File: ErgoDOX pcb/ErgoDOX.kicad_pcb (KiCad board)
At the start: 2 copper layers, 182.8 x 158.9 mm, 65 parts, among them J1 USB, J2 3.5mm, J3 JMP, J4 JMP, SW0:10 SW0:3, SW0:11 SW0:2, SW0:12 SW0:1, SW0:7 SW0:6, SW0:8 SW0:5, SW0:9 SW0:4, SW1:10 SW1:3, SW1:11 SW1:2, SW1:12 SW1:1, SW1:13 SW1:0, SW1:9 SW1:4, SW2:10 SW2:3, SW2:11 SW2:2, SW2:12 SW2:1, SW2:13 SW2:0, SW2:7 SW2:6, SW2:8 SW2:5, SW2:9 SW2:4, SW3:10 SW3:3, SW3:11 SW3:2, SW3:12 SW3:1, SW3:13 SW3:0, SW3:8 SW3:5, SW3:9 SW3:4, SW4:10 SW4:3, SW4:11 SW4:2, SW4:12 SW4:1, SW4:13 SW4:0, SW4:7 SW4:6, SW4:8 SW4:5, SW4:9 SW4:4, SW5:10 SW5:3, SW5:11 SW5:2, SW5:12 SW5:1, SW5:13 SW5:0, SW5:7 SW5:6, SW5:8 SW5:5, SW5:9 SW5:4, U1 TEENSY2.0, U2 MCP23018

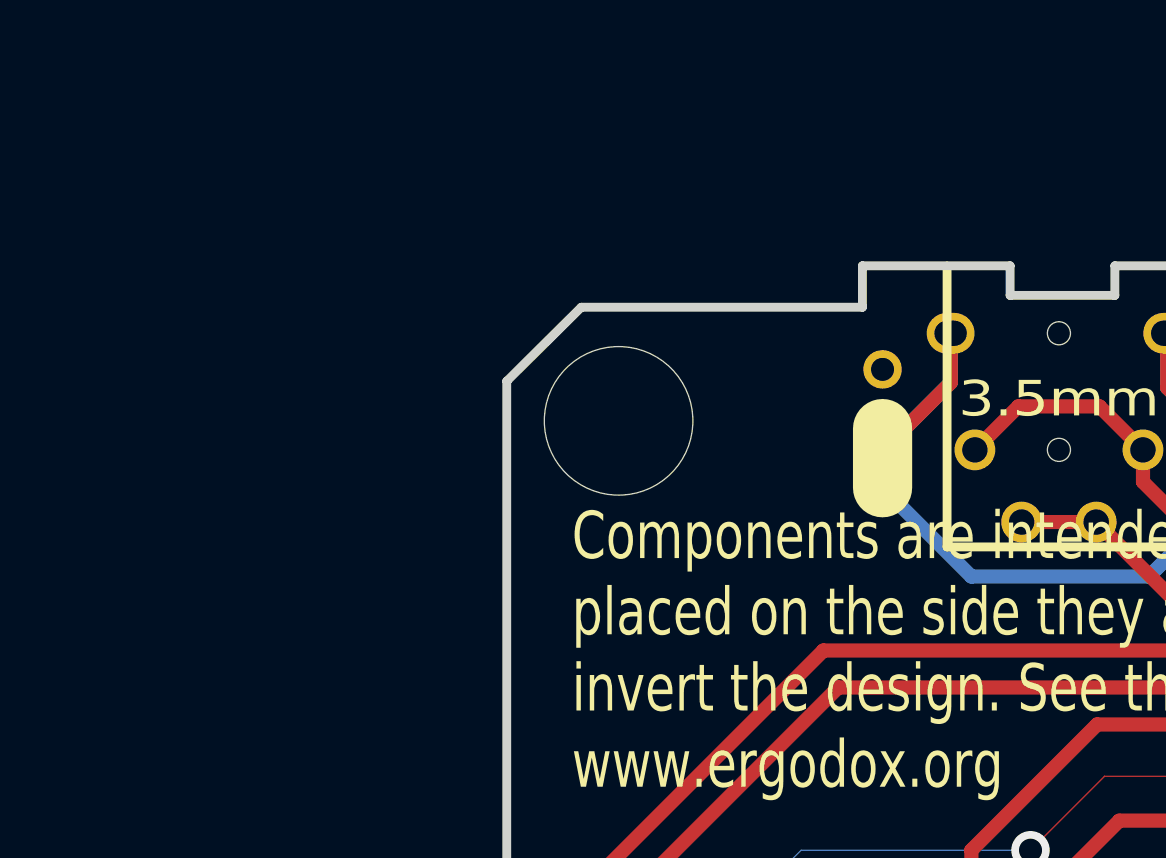
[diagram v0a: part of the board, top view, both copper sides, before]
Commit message: Add modules for LED
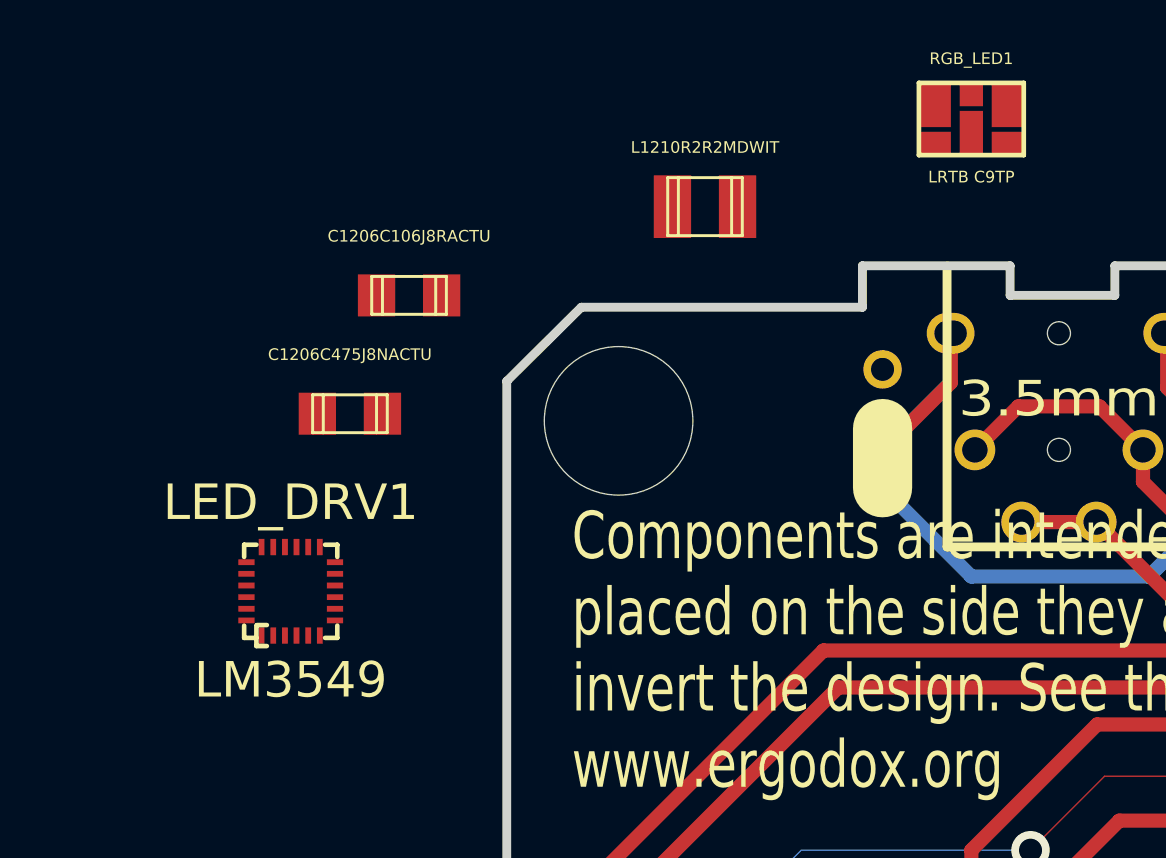
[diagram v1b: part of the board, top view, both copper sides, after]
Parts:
- added C1206C106J8RACTU: CIN, c_1206, F.Cu at (58.4, 31.8)
- added C1206C475J8NACTU: COUT, c_1206, F.Cu at (55.9, 36.8)
- added L1210R2R2MDWIT: L1, L_1210, F.Cu at (71.1, 27.9)
- added LM3549: LED_DRV1, LM3549, F.Cu at (53.3, 44.5)
- added LRTB C9TP: RGB_LED1, LRTB_C9TP, F.Cu at (82.5, 24.1)

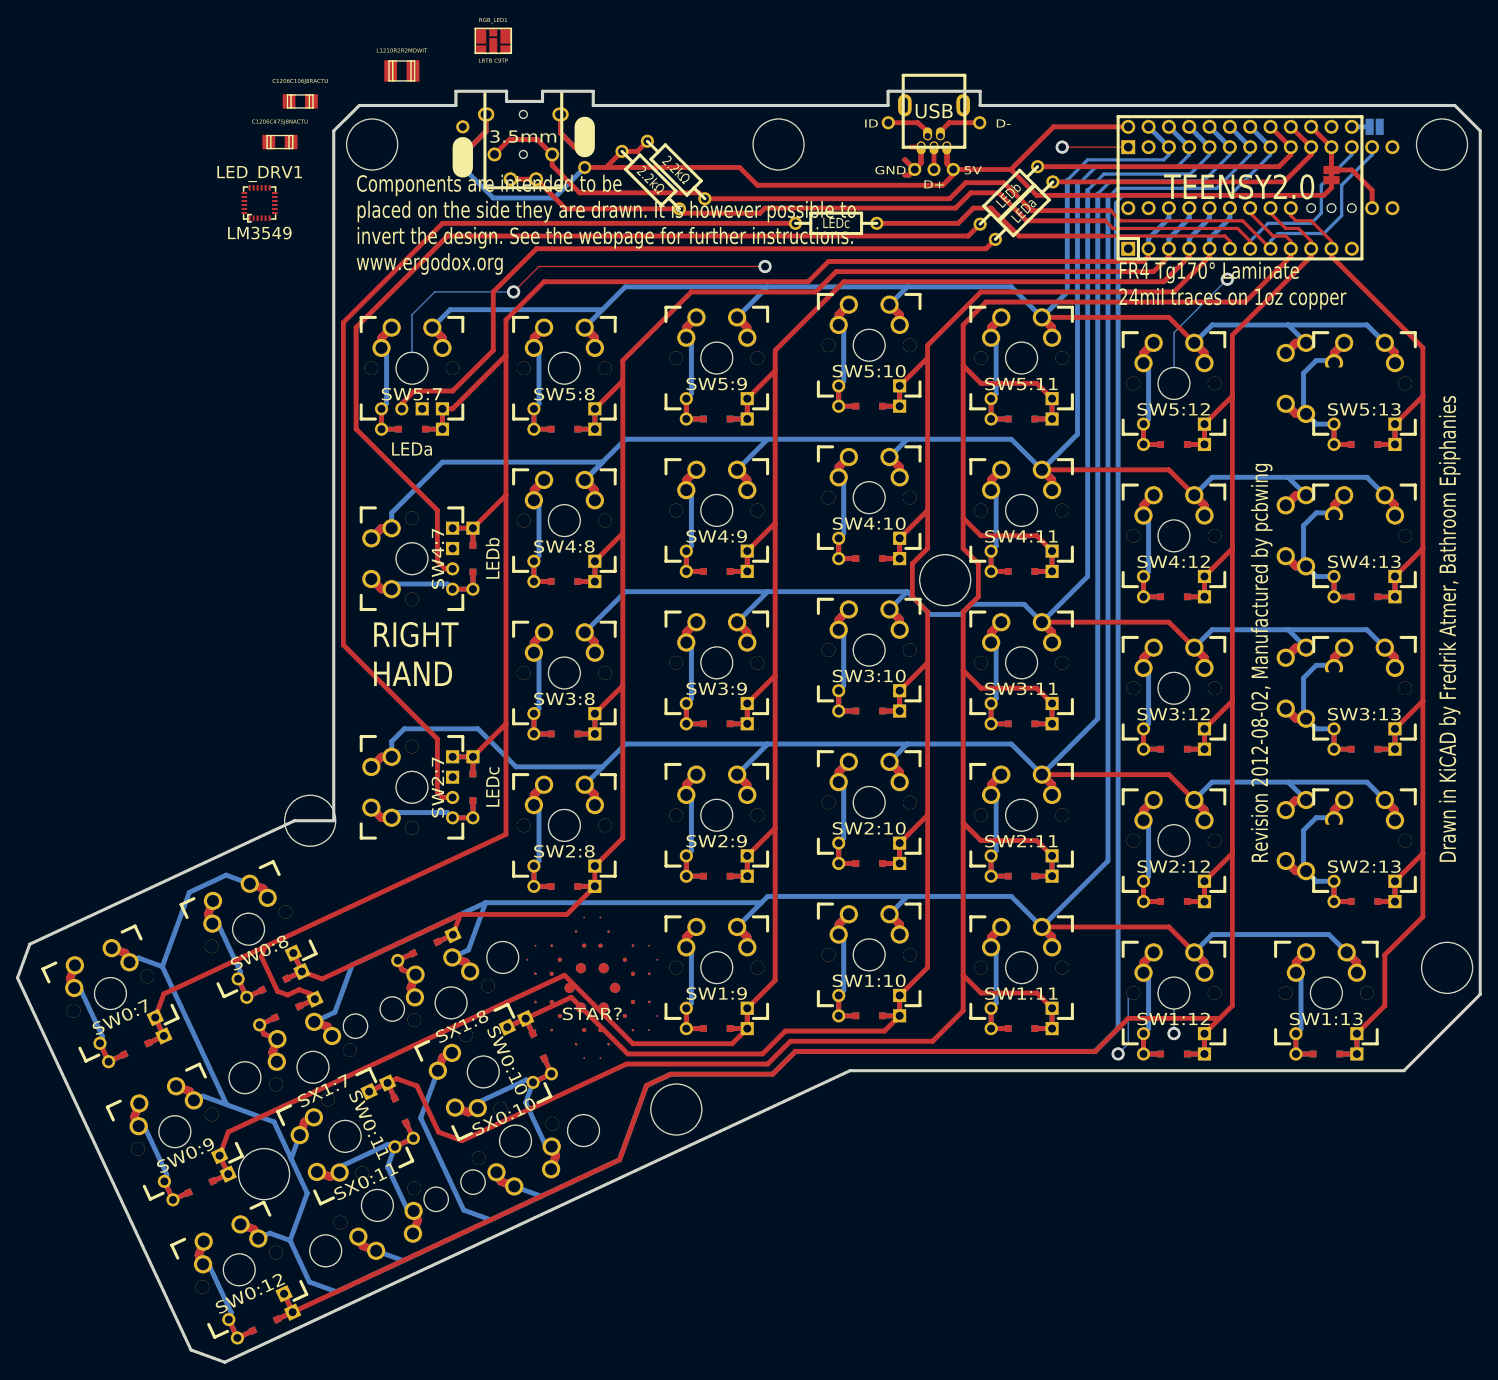
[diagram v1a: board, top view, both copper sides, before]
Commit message: More updates for backlight
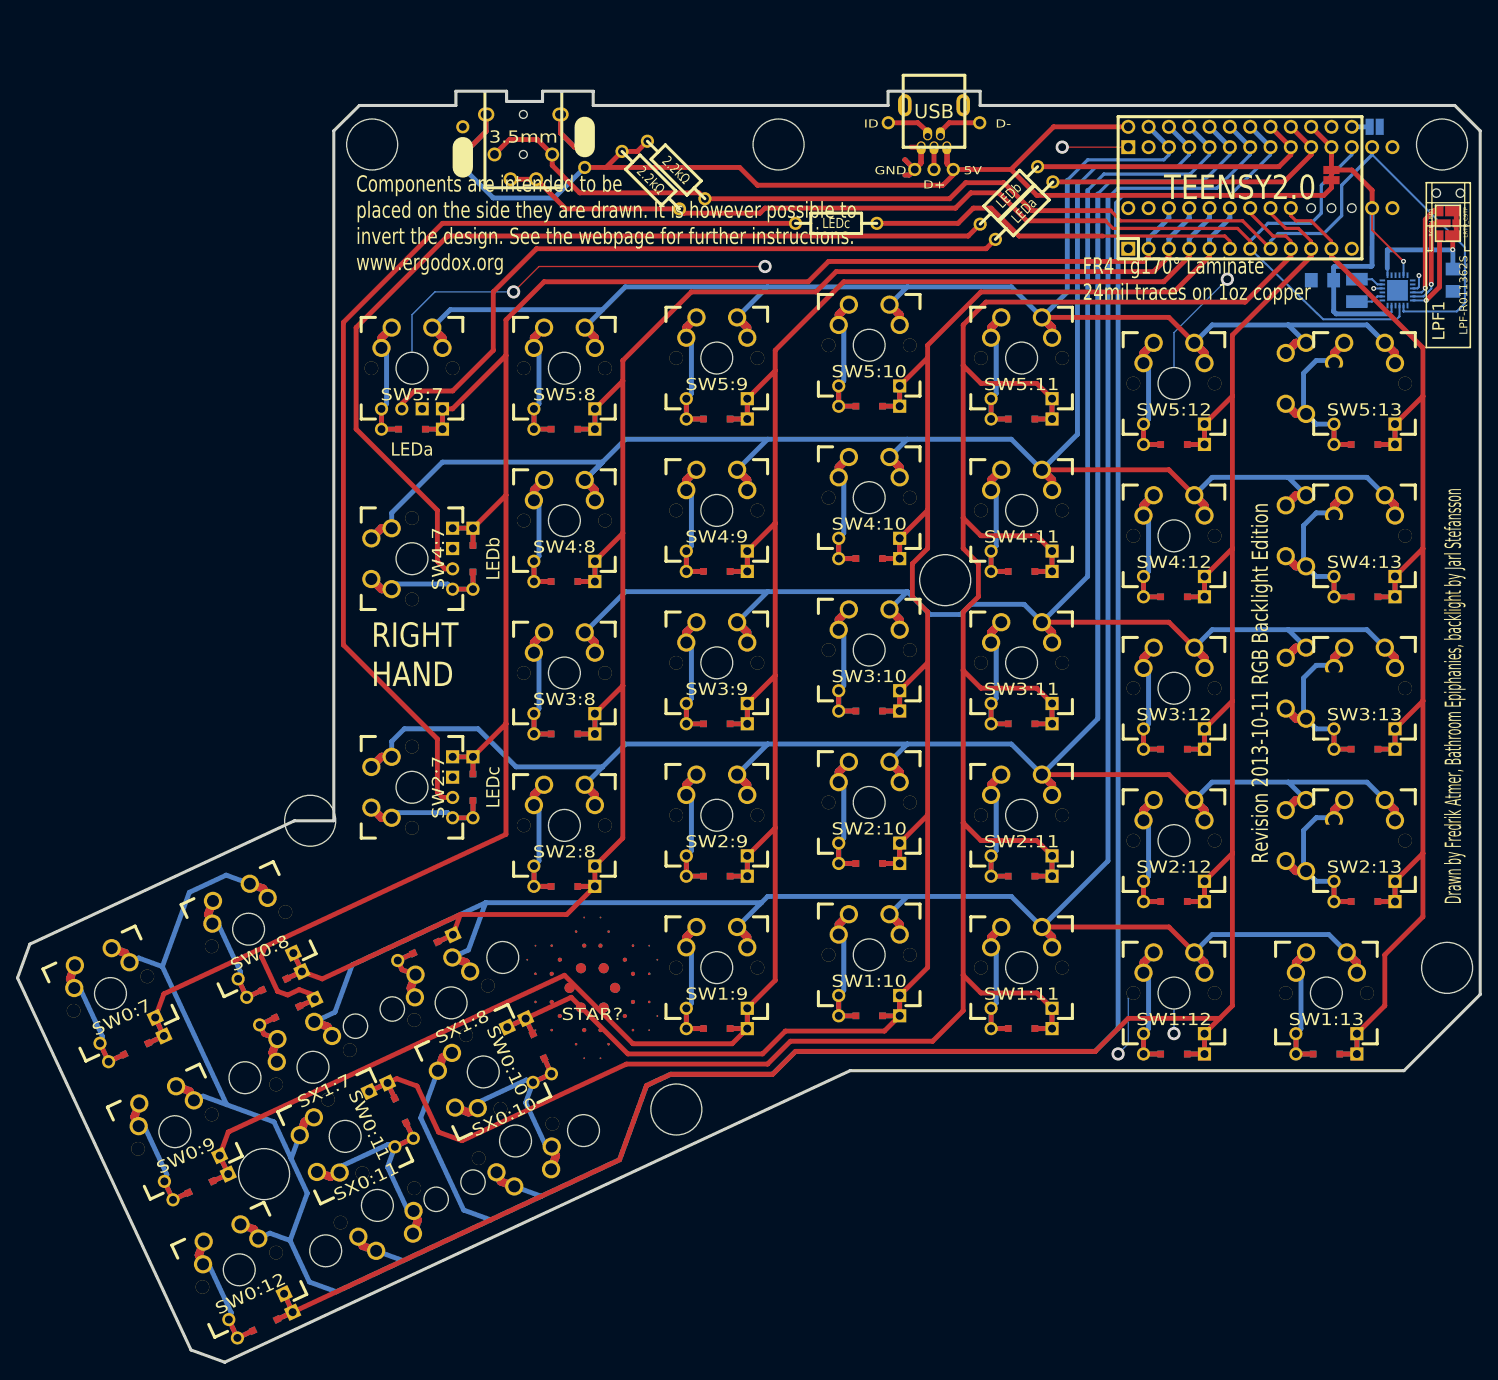
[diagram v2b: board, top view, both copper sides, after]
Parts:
- removed C1206C106J8RACTU: CIN, c_1206
- removed C1206C475J8NACTU: COUT, c_1206
- removed L1210R2R2MDWIT: L1, L_1210
- removed LM3549: LED_DRV1, LM3549
- removed LRTB C9TP: RGB_LED1, LRTB_C9TP
- added CIN1: CAP 10 µF,6.3V/10V X7R, C1206C106J8RACTU, B.Cu at (186.2, 54.1)
- added COUT1: CAP 4.7 µF, 6.3V/10V X7R, C1206C475J8NACTU, B.Cu at (202.5, 54.1)
- added L1: INDUCTOR 2.2 µH, 1900 mA, L1210R2R2MDWIT, B.Cu at (190.5, 55.4)
- added LED_DRV1: LM3549, LM3549, B.Cu at (195.6, 55.4)
- added LPF-R011362S: LPF1, LPF-R011362S, F.Cu at (201.9, 41.9)
- added RGB_LED1: LRTB_C9TP, LRTB_C9TP, F.Cu at (201.9, 47.0)
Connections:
- U1 pad 12: (no net) -> N-0000051
- U1 pad 19: (no net) -> N-0000052
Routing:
- net VCC: track 160.4 -> 196.3 mm, vias 0 -> 1
- net /SDAM: track 127.2 -> 160.4 mm
- net /SCLM: track 119.8 -> 143.6 mm
- net /V_OUT_C_CATHODE: track 0.00 -> 19.0 mm, vias 0 -> 1
- net /R_CATHODE: track 0.00 -> 12.7 mm, vias 0 -> 1
- net /G_CATHODE: track 0.00 -> 12.3 mm, vias 0 -> 1
- net /B_CATHODE: track 0.00 -> 10.5 mm, vias 0 -> 1
- net /L2_T1: track 0.00 -> 3.45 mm
- net /L1_T1: track 0.00 -> 3.45 mm
- net GND: track 104.3 -> 107.7 mm, vias 6 -> 8
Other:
- net class Default: clearance 0.3048 -> 0.127
- rule trace_clearance: 0.3048 -> 0.127
- board text added: "Drawn by Fredrik Atmer, Bathroom Epiphanies, backlight by Jarl Stefansson"
- board text added: "Revision 2013-10-11 RGB Backlight Edition"
- board text removed: "Drawn in KiCAD by Fredrik Atmer, Bathroom Epiphanies"
- board text removed: "Revision 2012-08-02, Manufactured by pcbwing"

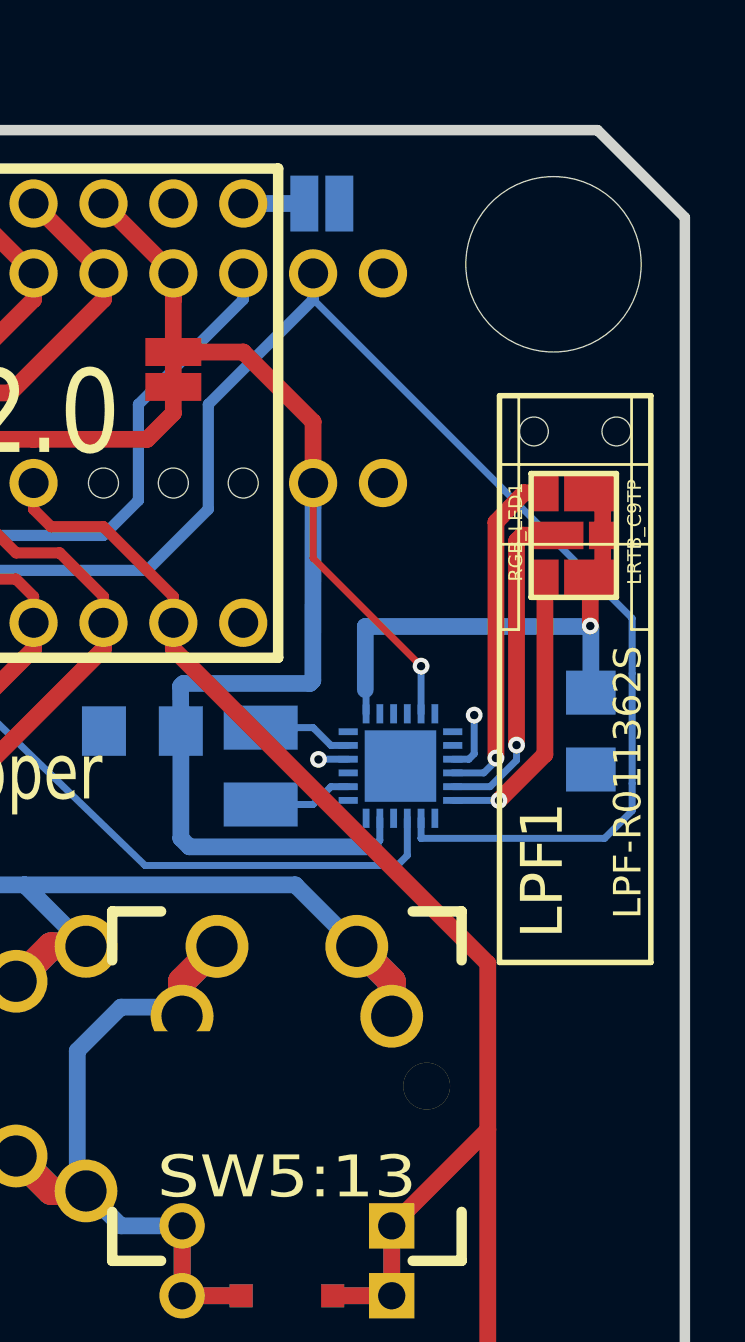
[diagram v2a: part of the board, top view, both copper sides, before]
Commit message: LED now available on both sides
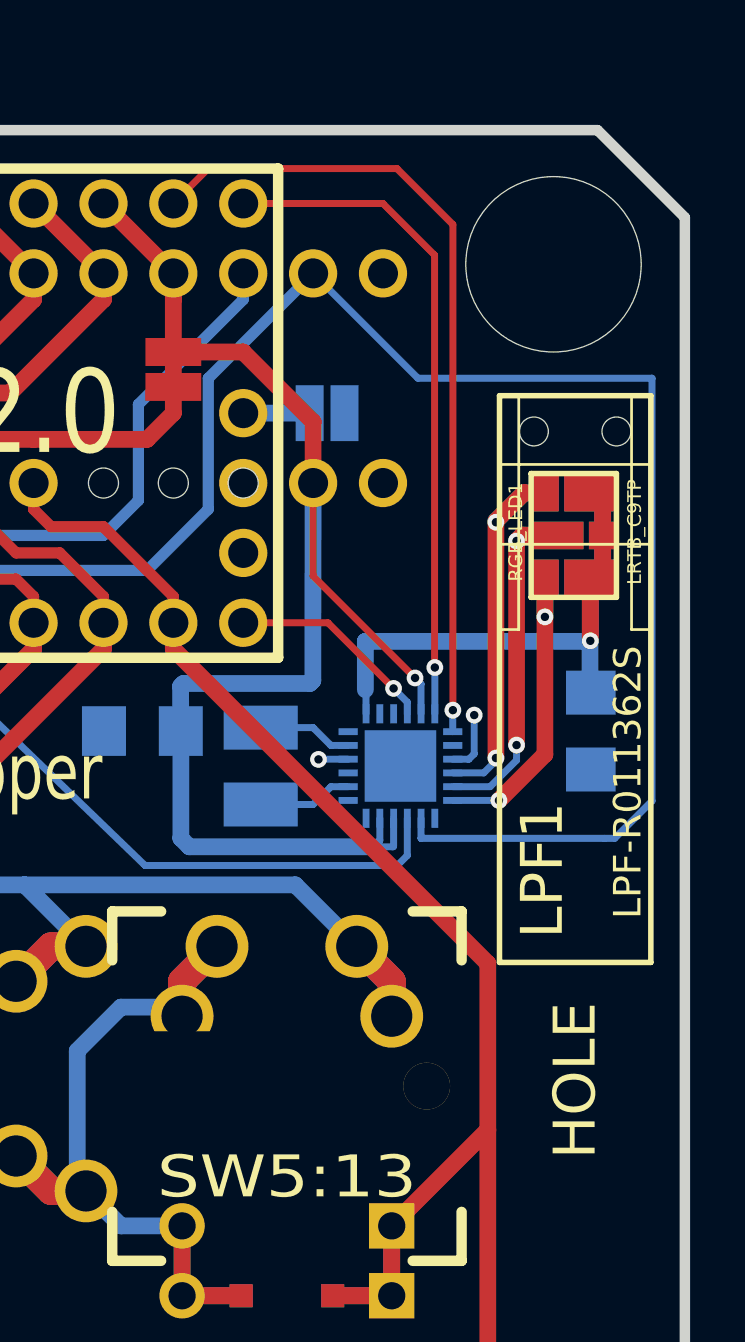
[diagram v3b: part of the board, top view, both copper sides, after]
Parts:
- added LRTB C9TP: RGB_LED1, LRTB_C9TP, B.Cu at (201.9, 47.0)
- moved JP2 7.62 mm to (192.9, 42.5)
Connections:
- CIN1 pad 1: GND -> (no net)
- COUT1 pad 1: GND -> (no net)
- LED_DRV1 pad 10: N-0000051 (its old number) -> /R_EN
- LED_DRV1 pad 12: N-0000052 -> /G_EN
- LED_DRV1 pad 13: (no net) -> /B_EN
- LED_DRV1 pad 22: (no net) -> VCC
- U1 pad 12: N-0000051 (its old number) -> /R_EN
- U1 pad 18: GND -> /G_EN
- U1 pad 19: N-0000052 -> /B_EN
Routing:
- net /B_EN: track 0.00 -> 30.0 mm, vias 0 -> 1
- net /G_EN: track 0.00 -> 24.4 mm, vias 0 -> 1
- net /R_EN: track 0.00 -> 7.58 mm, vias 0 -> 1
- net /SDAM: track 160.4 -> 166.5 mm
- net /V_OUT_C_CATHODE: track 19.0 -> 24.3 mm
- net /R_CATHODE: track 12.7 -> 14.9 mm, vias 1 -> 2
- net VCC: track 196.3 -> 198.1 mm
- net /G_CATHODE: track 12.3 -> 13.8 mm, vias 1 -> 2
- net /B_CATHODE: track 10.5 -> 11.9 mm, vias 1 -> 2
